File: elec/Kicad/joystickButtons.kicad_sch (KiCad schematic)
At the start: 0 parts

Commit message: merci Linux
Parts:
- added C1: 100nF, symbol Device:C
- added R1: 10K, symbol Device:R
- added SW1: SW_Push_BOOT, symbol Switch:SW_Push
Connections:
- new net +3V3: R1.1, SW1.1
- new net BOOT0: C1.1, SW1.2
- new net GND: C1.2, R1.2
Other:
- note added: "Exemple de pull-down qu'on devrait suivre"

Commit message: sa progresse. Battery management fini + humidity/temp sensor + bouton
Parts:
- added C7, C8: 100nF, symbol Device:C
- added R12, R13, R14: 10K, symbol Device:R
- added S1: SKRHABE010, SKRHABE01:SKRHABE010, symbol SKRHABE010:SKRHABE010
- added S2: 2765, 2765_Adafruit_Joystick:SW_2765, symbol 2765_Adafruit_Joystick:2765
- added SW2: SW_Push_Gauche_GO_BACK, symbol Switch:SW_Push
- added SW3: SW_Push_Gauche_LOG_EXIT, symbol Switch:SW_Push
- SW1: value SW_Push_BOOT -> SW_Push_Gauche_GO_IN
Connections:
- net +3V3: now also R13.1, R14.1, SW2.1, SW3.1
- net GND: now also C7.2, C8.2, R12.2, R13.2, R14.2, S1.5 (COMMON), S1.7, S1.8, S2.X-, S2.Y-
- net BOOT0 renamed PB11_Bouton_IN
- new net +3.3V: R12.1, S1.2 (CENTER), S1.4 (B), S1.6 (D), S2.X+, S2.Y+
- new net ADC1: S1.1 (A)
- new net ADC2: S1.3 (C)
- new net ADC_IN2: S2.X
- new net ADC_IN3: S2.Y
- new net PB10_Bouton_BACK: C7.1, SW2.2
- new net PB2_Bouton_LOG: C8.1, SW3.2
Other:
- note added: "En théorie, si on appuie sur le bouton, on devrai grounder le DigitalGPIO"
- note added: "Exemple de pull-down qu'on devrait suivre (PULL-DOWN)"
- note added: "La broche A et la broche C vont dans un ADC"
- note added: "Thumb joystick Adafruit (2765). Il n'y a pas de bouton"
- note added: "V1 thumb Joystick avec bouton (marche probablement pas laule)"
- note added: "click "log info" (ex: valeur de temp, distance...) / Exit de la magouille ultime"
- note added: "click droit / aller revenir d'une option (retourner dans le menu)"
- note added: "click gauche / aller sélectionner une option dans le menu"
- note added: "joystick: 1. soit juste un thumb stick (donc pas de bouton, mais on sait que cv marcher) 2. soit un genre de Alps SKRHABE01 qu'on sait pas si cv marcher mais il va dans les 5 directions donc, on aurait un bouton"
- note removed: "Exemple de pull-down qu'on devrait suivre"

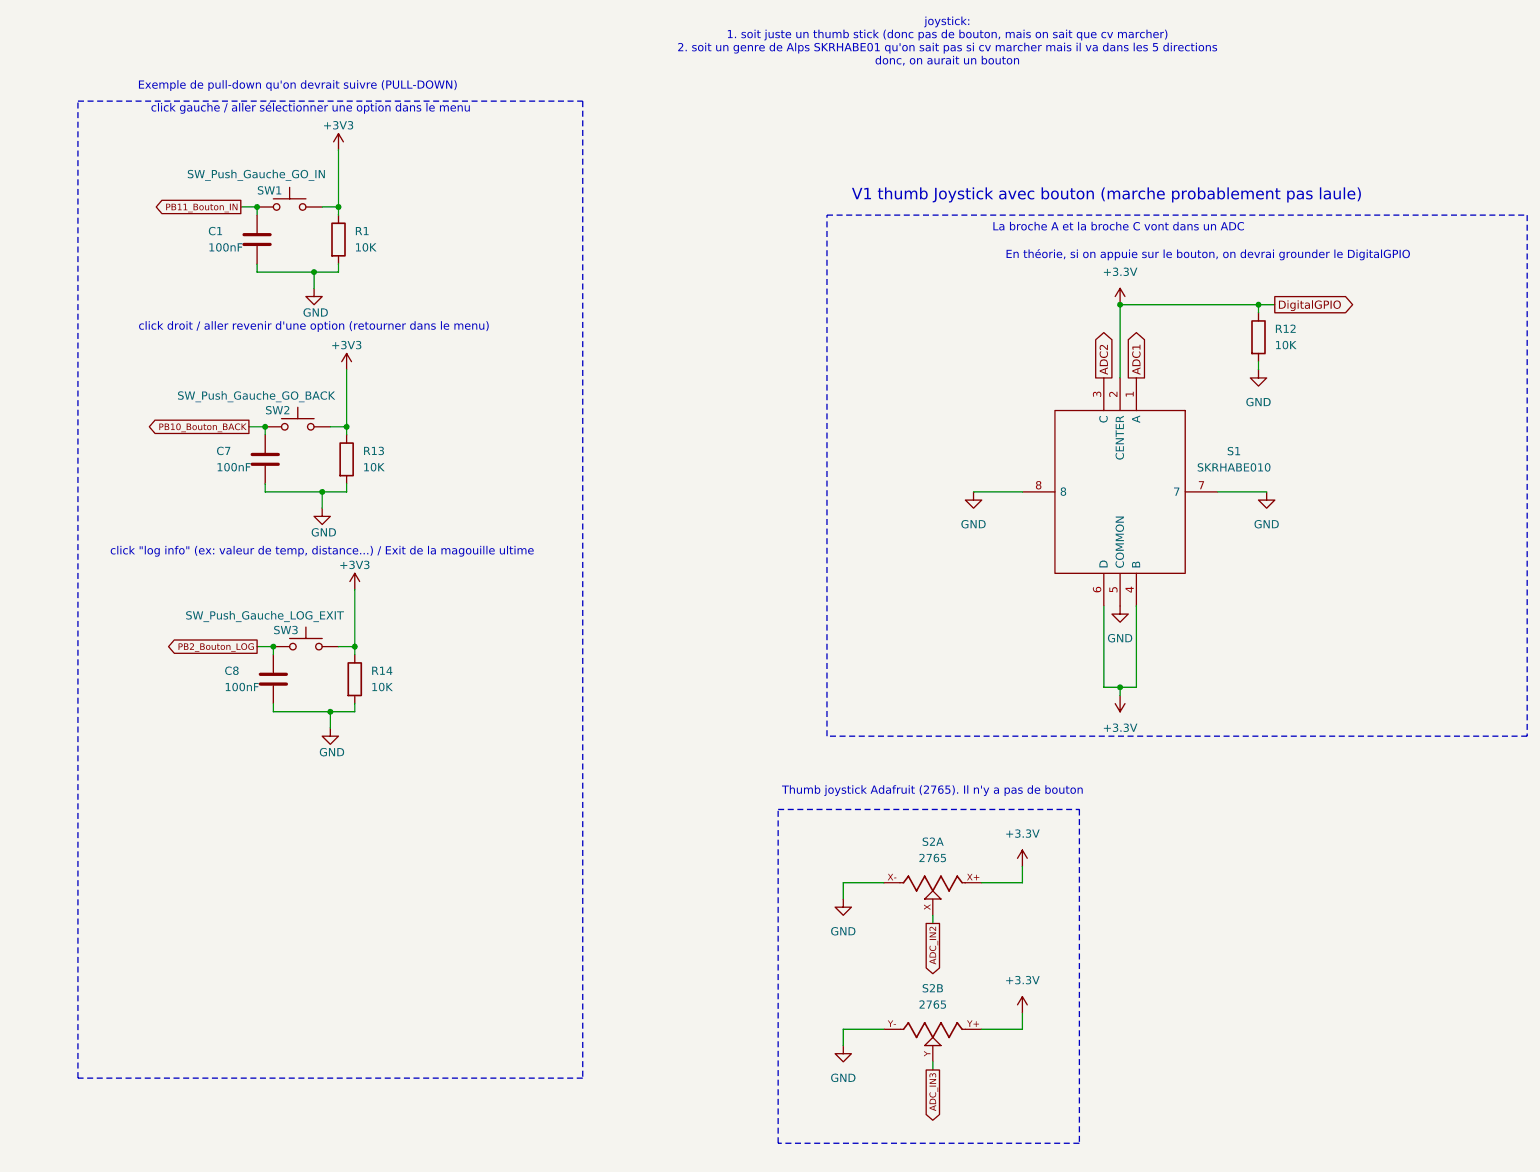
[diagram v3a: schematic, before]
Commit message: push pour charles (début de l'ajout diviseur tension pour la batterie)
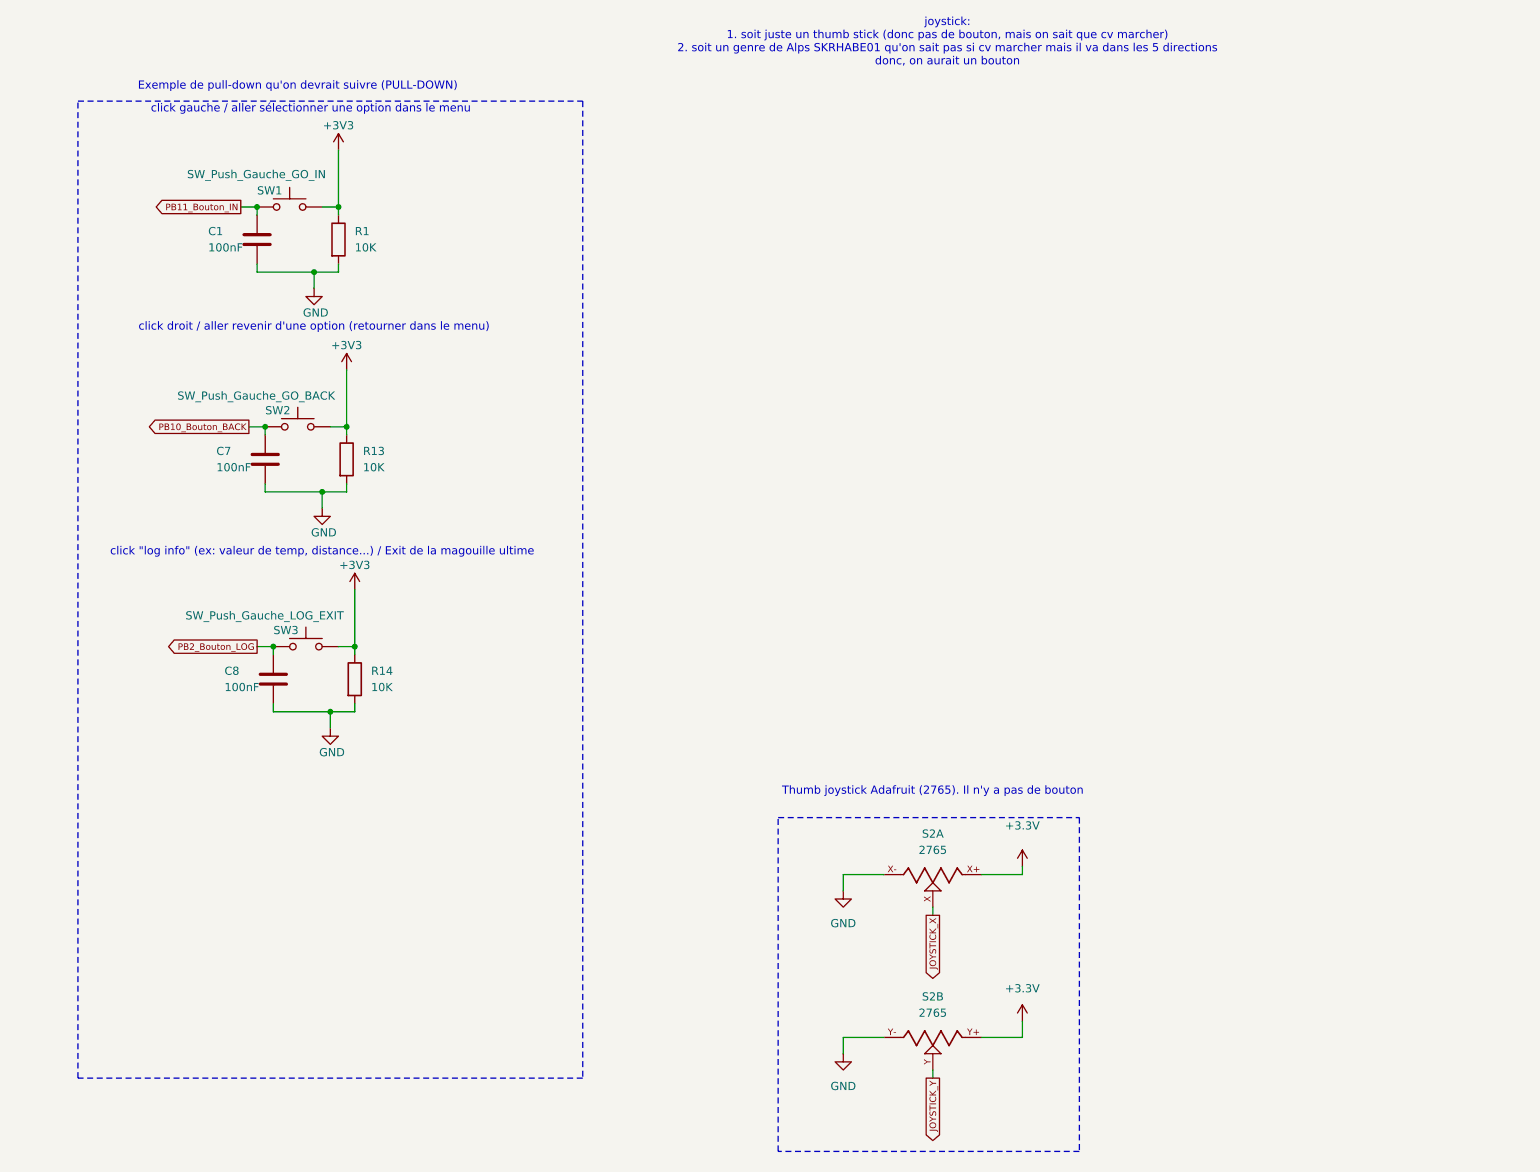
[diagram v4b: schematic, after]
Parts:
- removed R12: 10K, symbol Device:R
- removed S1: SKRHABE010, SKRHABE01:SKRHABE010, symbol SKRHABE010:SKRHABE010
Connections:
- net ADC_IN2 renamed JOYSTICK_X
- net ADC_IN3 renamed JOYSTICK_Y
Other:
- note removed: "En théorie, si on appuie sur le bouton, on devrai grounder le DigitalGPIO"
- note removed: "La broche A et la broche C vont dans un ADC"
- note removed: "V1 thumb Joystick avec bouton (marche probablement pas laule)"
- moved on the sheet: S2A, S2B

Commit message: push de magouille pour charles
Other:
- note added: "joystick: 1. soit juste un thumb stick (donc pas de bouton, mais on sait que cv marcher)"
- note removed: "joystick: 1. soit juste un thumb stick (donc pas de bouton, mais on sait que cv marcher) 2. soit un genre de Alps SKRHABE01 qu'on sait pas si cv marcher mais il va dans les 5 directions donc, on aurait un bouton"
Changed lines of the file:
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@@
 		)
 	)
-	(text "joystick:\n1. soit juste un thumb stick (donc pas de bouton, mais on sait que cv marcher)\n2. soit un genre de Alps SKRHABE01 qu'on sait pas si cv marcher mais il va dans les 5 directions\ndonc, on aurait un bouton\n"
+	(text "joystick:\n1. soit juste un thumb stick (donc pas de bouton, mais on sait que cv marcher)\n"
 		(exclude_from_sim no)
 		(at 154.686 20.066 0)

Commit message: add a few footprint
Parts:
- C1, C7, C8: footprint (none) -> Capacitor_SMD:C_0603_1608Metric_Pad1.08x0.95mm_HandSolder
- R1, R13, R14: footprint (none) -> Resistor_SMD:R_0603_1608Metric_Pad0.98x0.95mm_HandSolder
- SW1, SW2, SW3: footprint (none) -> Button_Switch_SMD:SW_SPST_PTS645
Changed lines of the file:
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@@
 			)
 		)
-		(property "Footprint" ""
+		(property "Footprint" "Resistor_SMD:R_0603_1608Metric_Pad0.98x0.95mm_HandSolder"
 			(at 60.452 119.38 90)
 			(effects
@@
 			)
 		)
-		(property "Footprint" ""
+		(property "Footprint" "Capacitor_SMD:C_0603_1608Metric_Pad1.08x0.95mm_HandSolder"
 			(at 50.4952 123.19 0)
 			(effects
@@
 			)
 		)
-		(property "Datasheet" "https://www.digikey.ca/en/products/detail/tdk-corporation/C2012X7S1A226M125AC/3951796"
+		(property "Datasheet" "https://www.digikey.ca/en/products/detail/yageo/CC0603KRX7R7BB104/302822"
 			(at 49.53 119.38 0)
 			(effects
@@
 			)
 		)
-		(property "Footprint" ""
+		(property "Footprint" "Button_Switch_SMD:SW_SPST_PTS645"
 			(at 54.61 109.22 0)
 			(effects
@@
 			)
 		)
-		(property "Footprint" ""
+		(property "Footprint" "Button_Switch_SMD:SW_SPST_PTS645"
 			(at 52.07 40.64 0)
 			(effects
@@
 			)
 		)
-		(property "Footprint" ""
+		(property "Footprint" "Capacitor_SMD:C_0603_1608Metric_Pad1.08x0.95mm_HandSolder"
 			(at 49.2252 88.9 0)
 			(effects
@@
 			)
 		)
-		(property "Datasheet" "https://www.digikey.ca/en/products/detail/tdk-corporation/C2012X7S1A226M125AC/3951796"
+		(property "Datasheet" "https://www.digikey.ca/en/products/detail/yageo/CC0603KRX7R7BB104/302822"
 			(at 48.26 85.09 0)
 			(effects
@@
 			)
 		)
-		(property "Footprint" ""
+		(property "Footprint" "Capacitor_SMD:C_0603_1608Metric_Pad1.08x0.95mm_HandSolder"
 			(at 47.9552 54.61 0)
 			(effects
@@
 			)
 		)
-		(property "Datasheet" "https://www.digikey.ca/en/products/detail/tdk-corporation/C2012X7S1A226M125AC/3951796"
+		(property "Datasheet" "https://www.digikey.ca/en/products/detail/yageo/CC0603KRX7R7BB104/302822"
 			(at 46.99 50.8 0)
 			(effects
@@
 			)
 		)
-		(property "Footprint" ""
+		(property "Footprint" "Resistor_SMD:R_0603_1608Metric_Pad0.98x0.95mm_HandSolder"
 			(at 57.912 50.8 90)
 			(effects
@@
 			)
 		)
-		(property "Footprint" ""
+		(property "Footprint" "Button_Switch_SMD:SW_SPST_PTS645"
 			(at 53.34 74.93 0)
 			(effects
@@
 			)
 		)
-		(property "Footprint" ""
+		(property "Footprint" "Resistor_SMD:R_0603_1608Metric_Pad0.98x0.95mm_HandSolder"
 			(at 59.182 85.09 90)
 			(effects

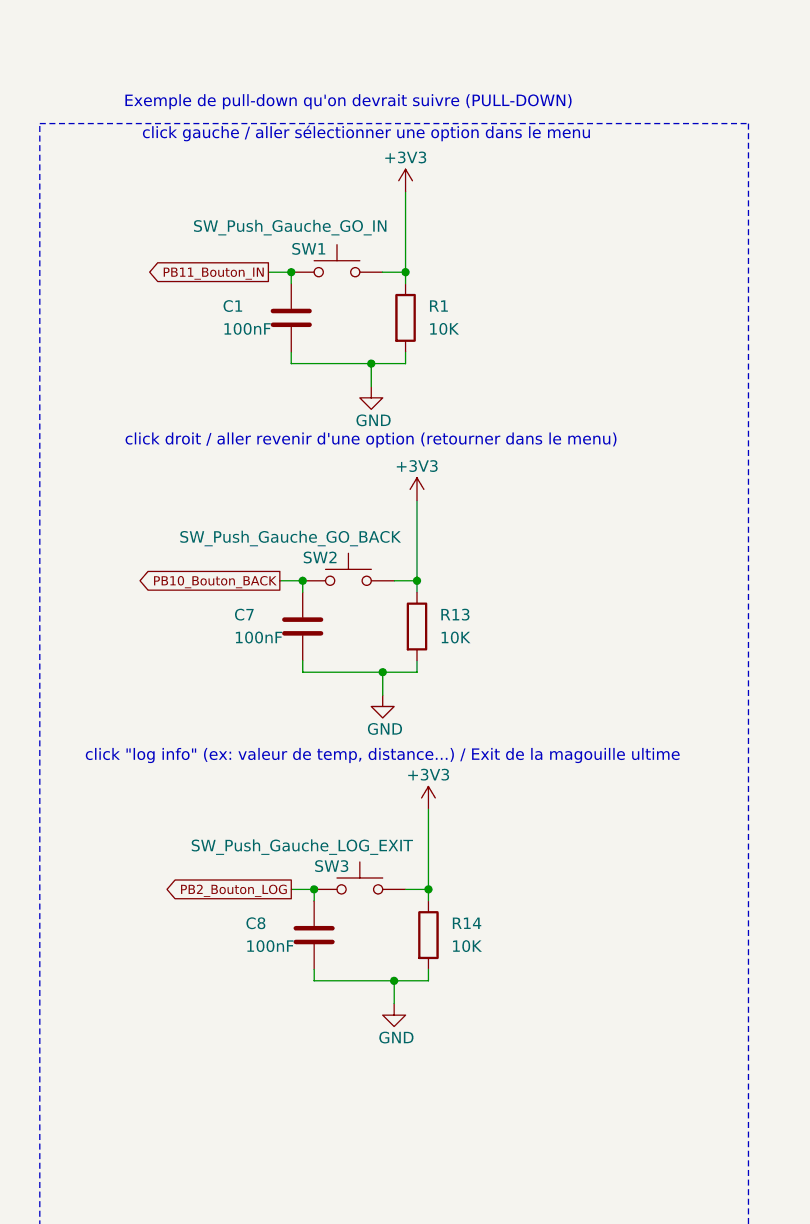
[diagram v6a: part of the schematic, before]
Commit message: ajout d'un Mosfet de type N pour pouvoir gérer le % de batterie (ADC)
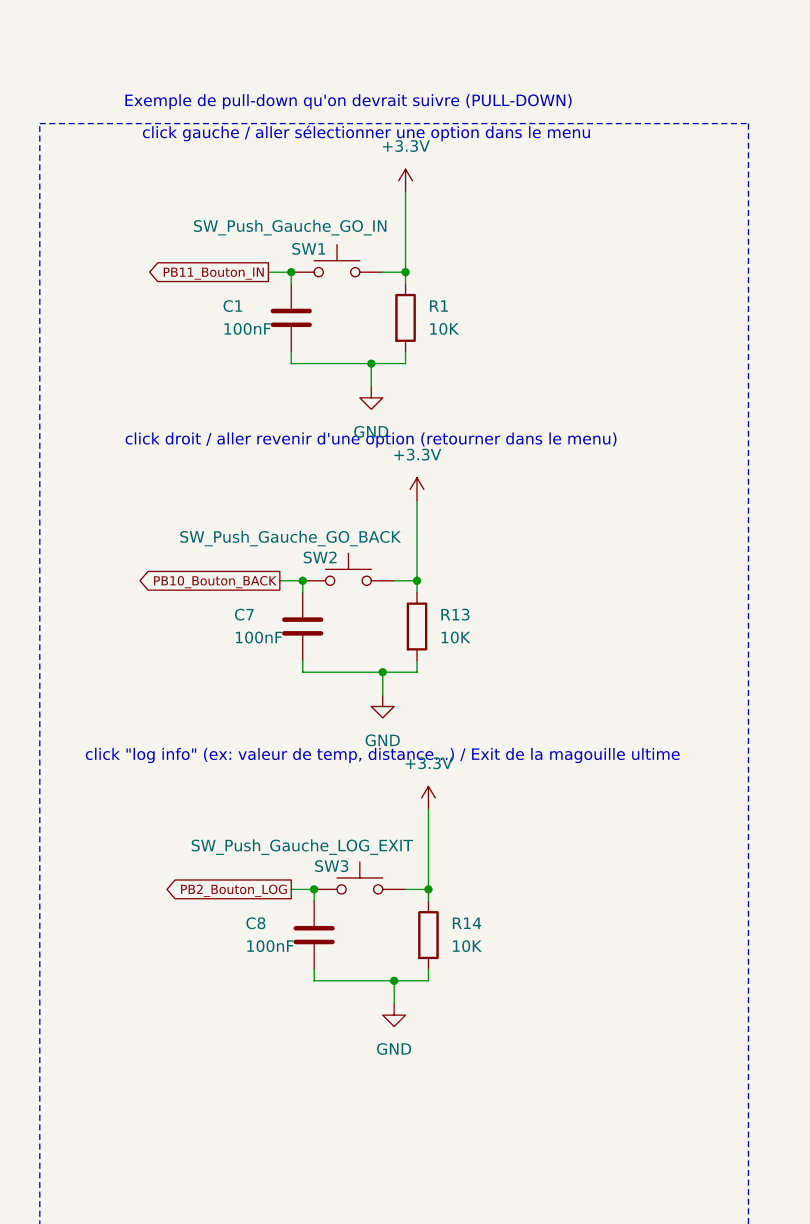
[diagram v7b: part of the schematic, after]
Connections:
- net +3V3 is gone; now on net +3.3V: R1.1, R13.1, R14.1, SW1.1, SW2.1, SW3.1

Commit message: commencer le PCB vite fait
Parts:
- SW2: value SW_Push_Gauche_GO_BACK -> SW_Push_Droite_GO_BACK
- SW3: value SW_Push_Gauche_LOG_EXIT -> SW_Push_Action_LOG_EXIT
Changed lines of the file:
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@@
 			)
 		)
-		(property "Value" "SW_Push_Gauche_LOG_EXIT"
+		(property "Value" "SW_Push_Action_LOG_EXIT"
 			(at 35.814 109.474 0)
 			(effects
@@
 			)
 		)
-		(property "Value" "SW_Push_Gauche_GO_BACK"
+		(property "Value" "SW_Push_Droite_GO_BACK"
 			(at 34.544 75.184 0)
 			(effects
